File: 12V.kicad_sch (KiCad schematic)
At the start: 0 parts

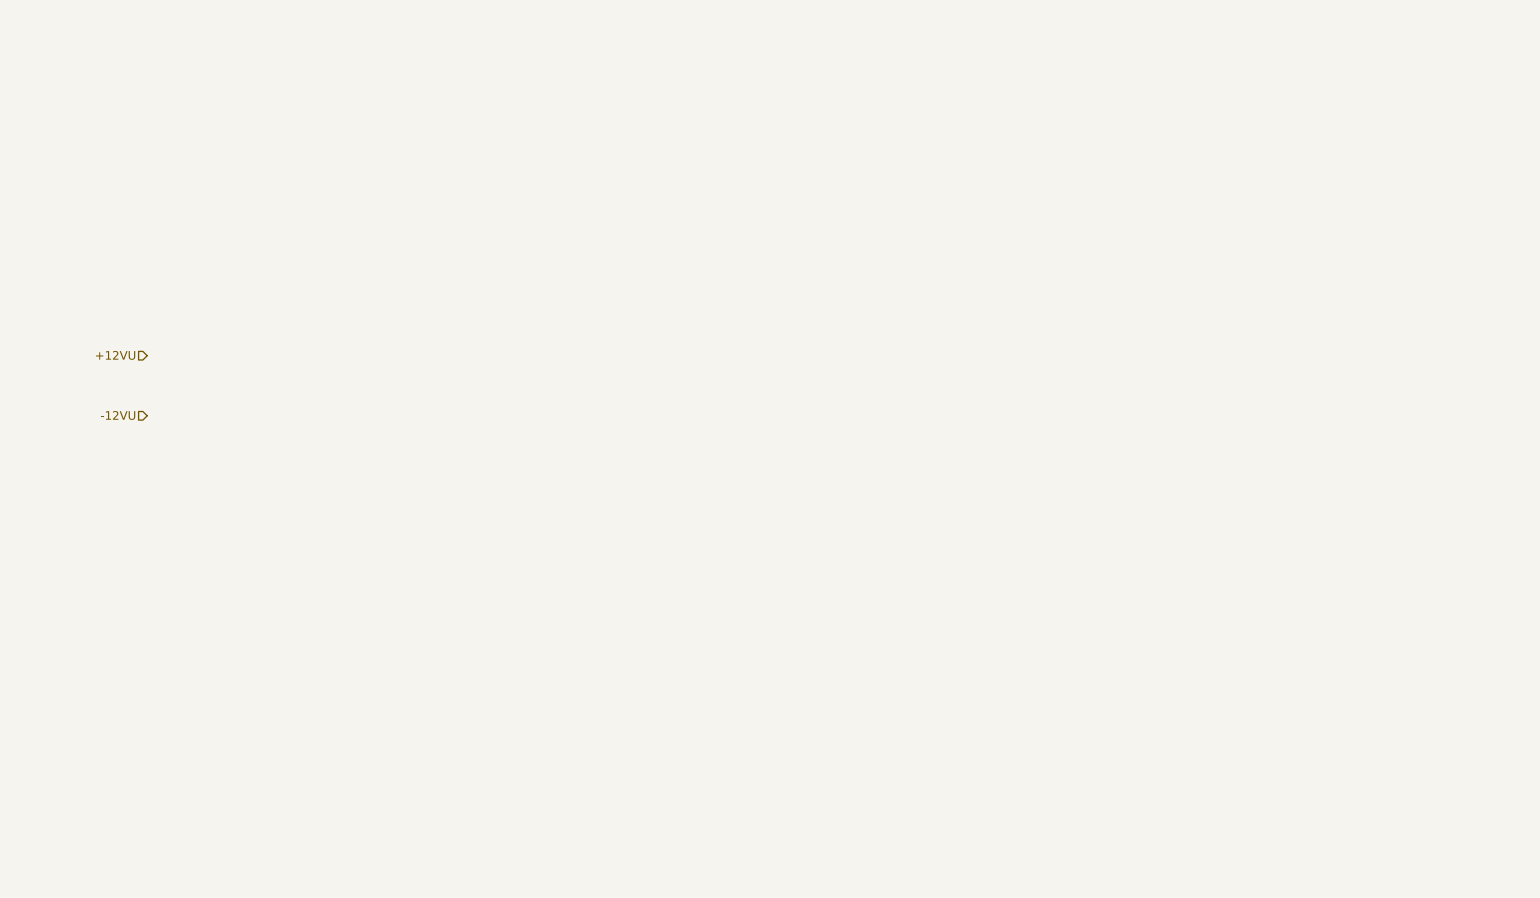
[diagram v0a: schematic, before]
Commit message: Schematic should be finished at this point.  Added more commentary to the README, and ensured all components have footprints assigned.
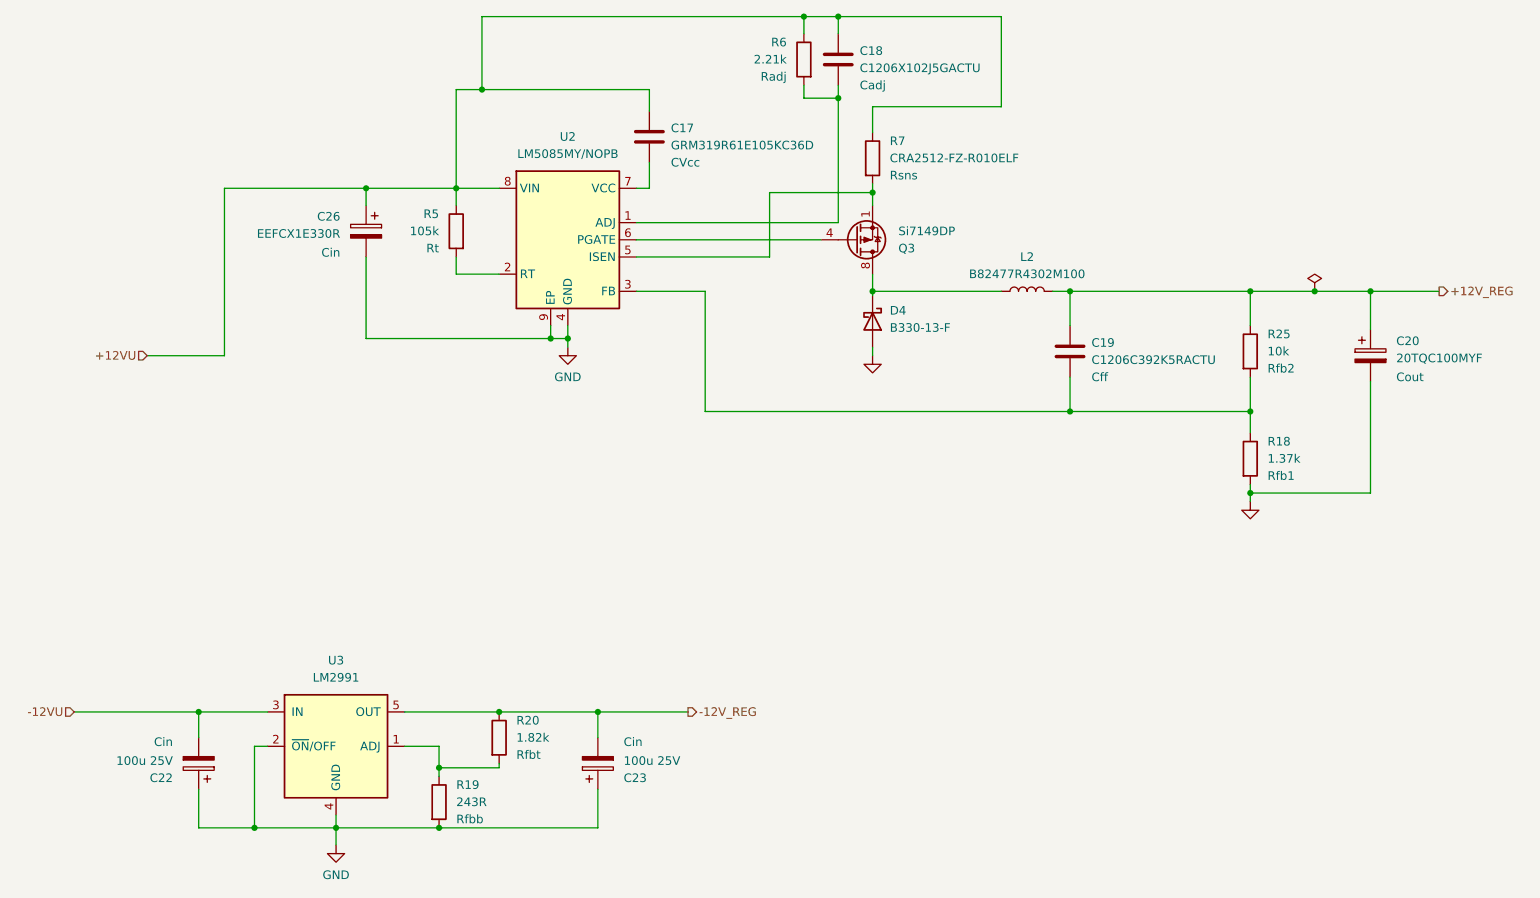
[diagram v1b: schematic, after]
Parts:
- added C17: GRM319R61E105KC36D, Capacitor_SMD:C_1206_3216Metric_Pad1.33x1.80mm_HandSolder, symbol Device:C
- added C18: C1206X102J5GACTU, Capacitor_SMD:C_1206_3216Metric_Pad1.33x1.80mm_HandSolder, symbol Device:C
- added C19: C1206C392K5RACTU, Capacitor_SMD:C_1206_3216Metric_Pad1.33x1.80mm_HandSolder, symbol Device:C
- added C20: 20TQC100MYF, Capacitor_Tantalum_SMD:CP_EIA-7343-20_Kemet-V_Pad2.25x2.55mm_HandSolder, symbol Device:C_Polarized
- added C22, C23: 100u 25V, Capacitor_THT:CP_Radial_D6.3mm_P2.50mm, symbol Device:C_Polarized
- added C26: EEFCX1E330R, Capacitor_Tantalum_SMD:CP_EIA-7343-20_Kemet-V_Pad2.25x2.55mm_HandSolder, symbol Device:C_Polarized
- added D4: B330-13-F, Diode_SMD:D_SMC, symbol Diode:B330
- added L2: B82477R4302M100, Inductor_SMD:L_TDK_SLF12555, symbol Device:L
- added Q3: Si7149DP, Package_SO:PowerPAK_SO-8_Single, symbol Device:Q_PMOS_DGS
- added R18: 1.37k, Resistor_SMD:R_1206_3216Metric_Pad1.30x1.75mm_HandSolder, symbol Device:R
- added R19: 243R, Resistor_SMD:R_1206_3216Metric_Pad1.30x1.75mm_HandSolder, symbol Device:R
- added R20: 1.82k, Resistor_SMD:R_1206_3216Metric_Pad1.30x1.75mm_HandSolder, symbol Device:R
- added R25: 10k, Resistor_SMD:R_1206_3216Metric_Pad1.30x1.75mm_HandSolder, symbol Device:R
- added R5: 105k, Resistor_SMD:R_1206_3216Metric_Pad1.30x1.75mm_HandSolder, symbol Device:R
- added R6: 2.21k, Resistor_SMD:R_1206_3216Metric_Pad1.30x1.75mm_HandSolder, symbol Device:R
- added R7: CRA2512-FZ-R010ELF, Resistor_SMD:R_2512_6332Metric_Pad1.40x3.35mm_HandSolder, symbol Device:R
- added U2: LM5085MY/NOPB, Package_SO:HVSSOP-8-1EP_3x3mm_P0.65mm_EP1.57x1.89mm_ThermalVias, symbol Regulator_Switching:LM25085MY
- added U3: LM2991, Package_TO_SOT_THT:TO-220-5_Vertical, symbol Regulator_Linear:LM2990SX-12
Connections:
- net +12VU: now also C17.1, C18.1, C26.1, R5.1, R6.1, R7.1, U2.8 (VIN)
- net -12VU: now also C22.2, U3.3 (IN)
- new net: R19.1, R20.2, U3.1 (ADJ)
- new net: D4.1 (K), L2.1, Q3.5 (D), Q3.6 (D), Q3.7 (D), Q3.8 (D)
- new net: C19.2, R18.1, R25.2, U2.3 (FB)
- new net: R5.2, U2.2 (RT)
- new net: C17.2, U2.7 (VCC)
- new net: C18.2, R6.2, U2.1 (ADJ)
- new net: Q3.1 (S), Q3.2 (S), Q3.3 (S), R7.2, U2.5 (ISEN)
- new net: Q3.4 (G), U2.6 (PGATE)
- new net +12V_REG: C19.1, C20.1, L2.2, R25.1
- new net -12V_REG: C23.2, R20.1, U3.5 (OUT)
- new net GND: C20.2, C22.1, C23.1, C26.2, D4.2 (A), R18.2, R19.2, U2.4 (GND), U2.9 (EP), U3.2 (~{ON}/OFF), U3.4 (GND)

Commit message: Finished schematic; began placing and routing board. 12V regulation section still not placed, and HV section not routed.
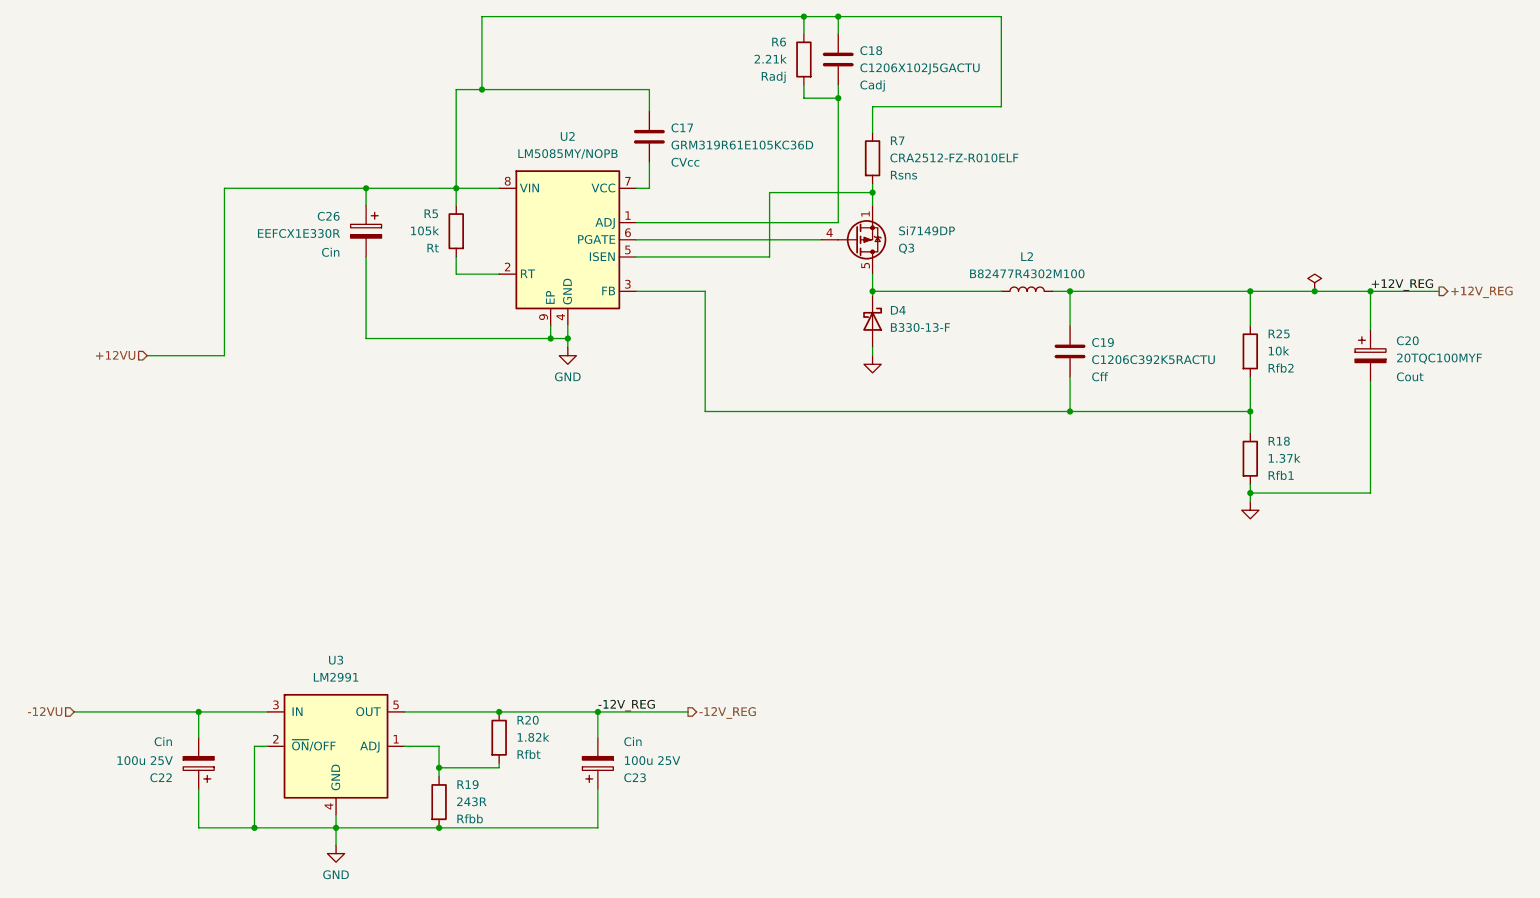
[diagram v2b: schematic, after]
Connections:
- net at D4.1 (K), L2.1, Q3.5 (D): no longer Q3.6 (D), Q3.7 (D), Q3.8 (D)
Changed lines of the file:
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@@
+		)
+	)
+	(label "+12V_REG"
+		(at 251.46 66.04 0)
+		(fields_autoplaced yes)
+		(effects
+			(font
+				(size 1.27 1.27)
+			)
+			(justify left bottom)
+		)
+		(property "Netclass" "LV_HC"
+			(at 251.46 67.31 0)
+			(effects
+				(font
+					(size 1.27 1.27)
+					(italic yes)
+				)
+				(justify left)
+				(hide yes)
+			)
+		)
+	)
+	(label "-12V_REG"
+		(at 137.16 128.27 0)
+		(fields_autoplaced yes)
+		(effects
+			(font
+				(size 1.27 1.27)
+			)
+			(justify left bottom)
+		)
+		(property "Netclass" "LV_LC"
+			(at 137.16 129.54 0)
+			(effects
+				(font
+					(size 1.27 1.27)
+					(italic yes)
+				)
+				(justify left)
+				(hide yes)
+			)
 		)
 	)
@@
 		(pin "5"
 		)
-		(pin "8"
-		)
-		(pin "7"
-		)
-		(pin "6"
-		)
 		(pin "4"

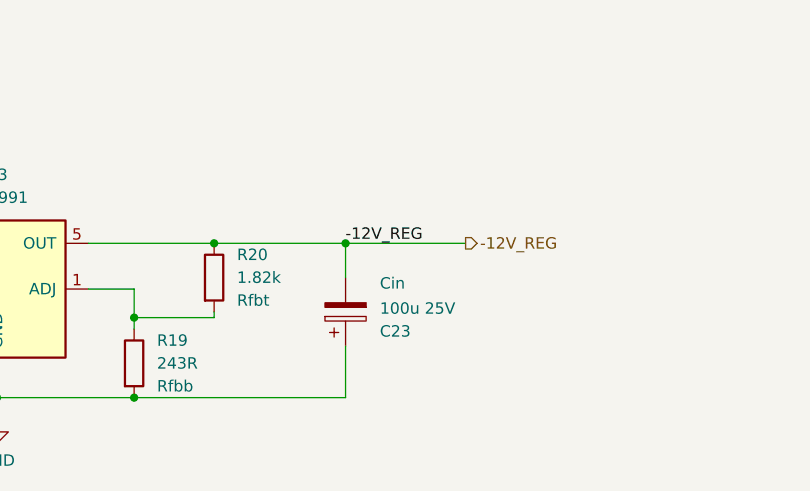
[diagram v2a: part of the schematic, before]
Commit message: Finished routing. While DRC fails with some errors, some can be disregarded. Need to do some cleanups to get rid of the others.
Also, added 3 discharge resistors to the schematic.
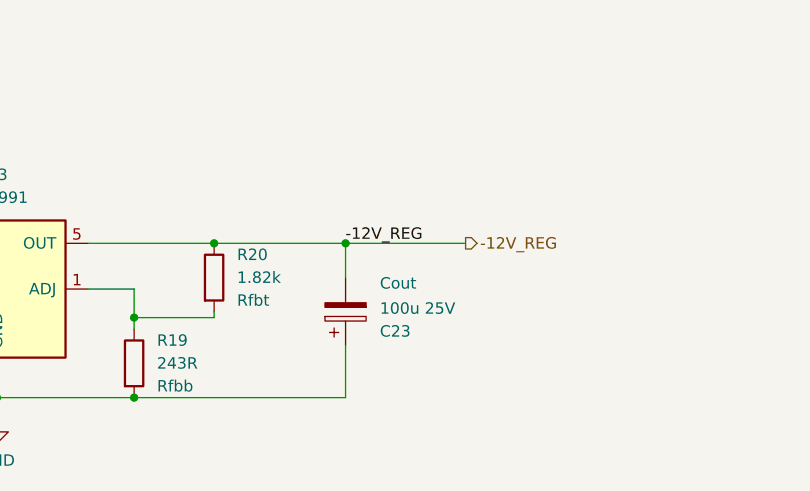
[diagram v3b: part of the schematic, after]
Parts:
- C23: Designator Cin -> Cout
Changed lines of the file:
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@@
 			)
 		)
-		(property "Designator" "Cin"
+		(property "Designator" "Cout"
 			(at 140.97 132.715 0)
 			(effects
